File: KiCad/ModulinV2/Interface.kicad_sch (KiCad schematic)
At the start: 46 parts, among them IC3 ADS7041IDCUR, IC4 ADS7041IDCUR, IC5 ADS7866IDBVT, IC6 ADS7866IDBVT, IC7 DAC60501ZDGSR, IC8 DAC60501ZDGSR

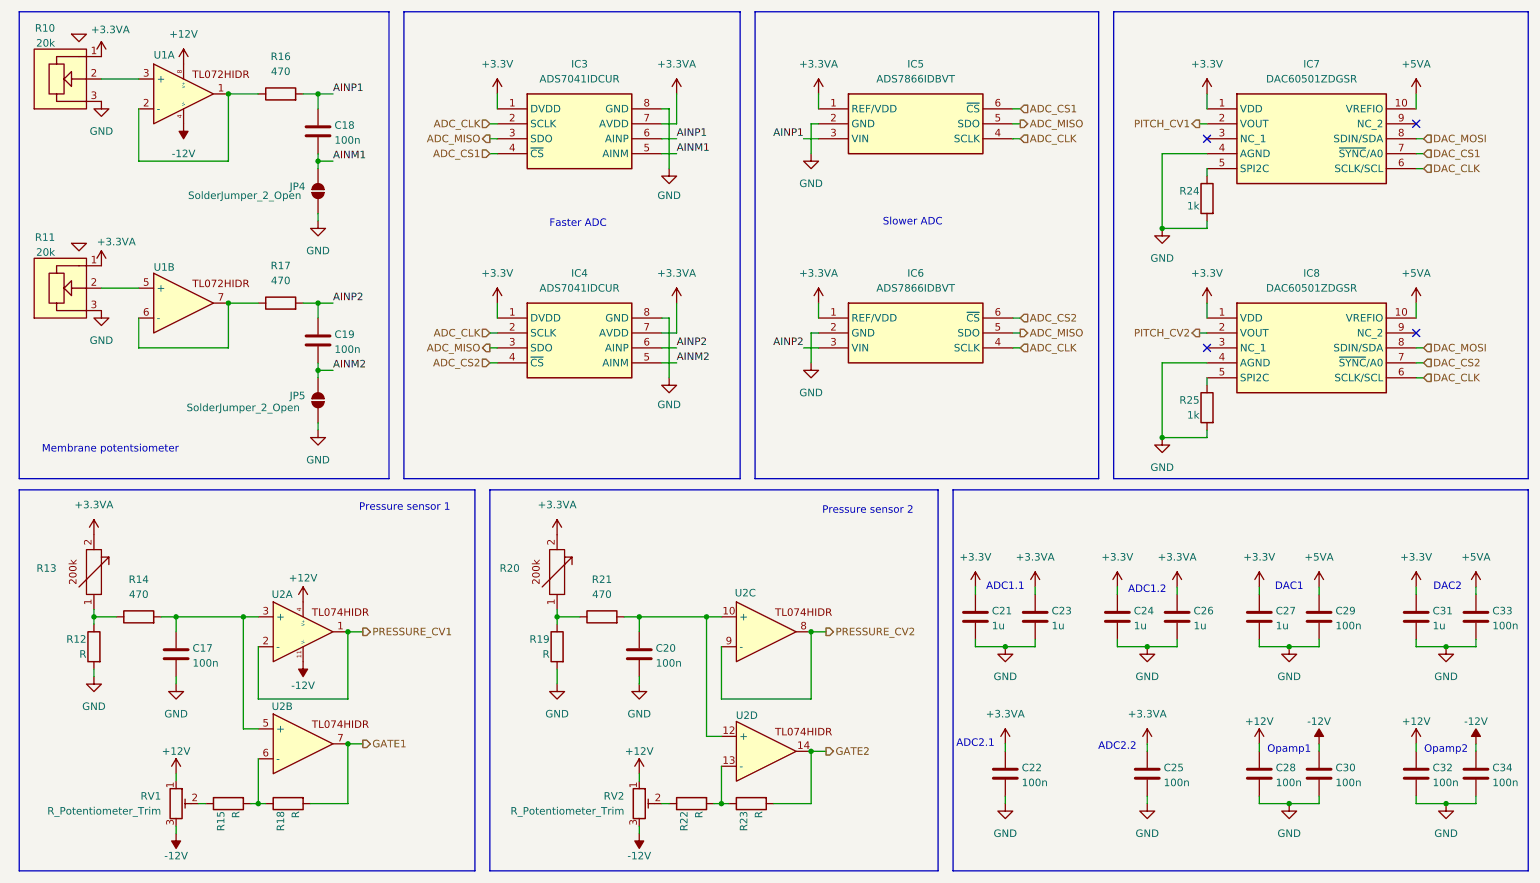
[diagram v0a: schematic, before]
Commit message: Added 4k7 pullups to I2C lines
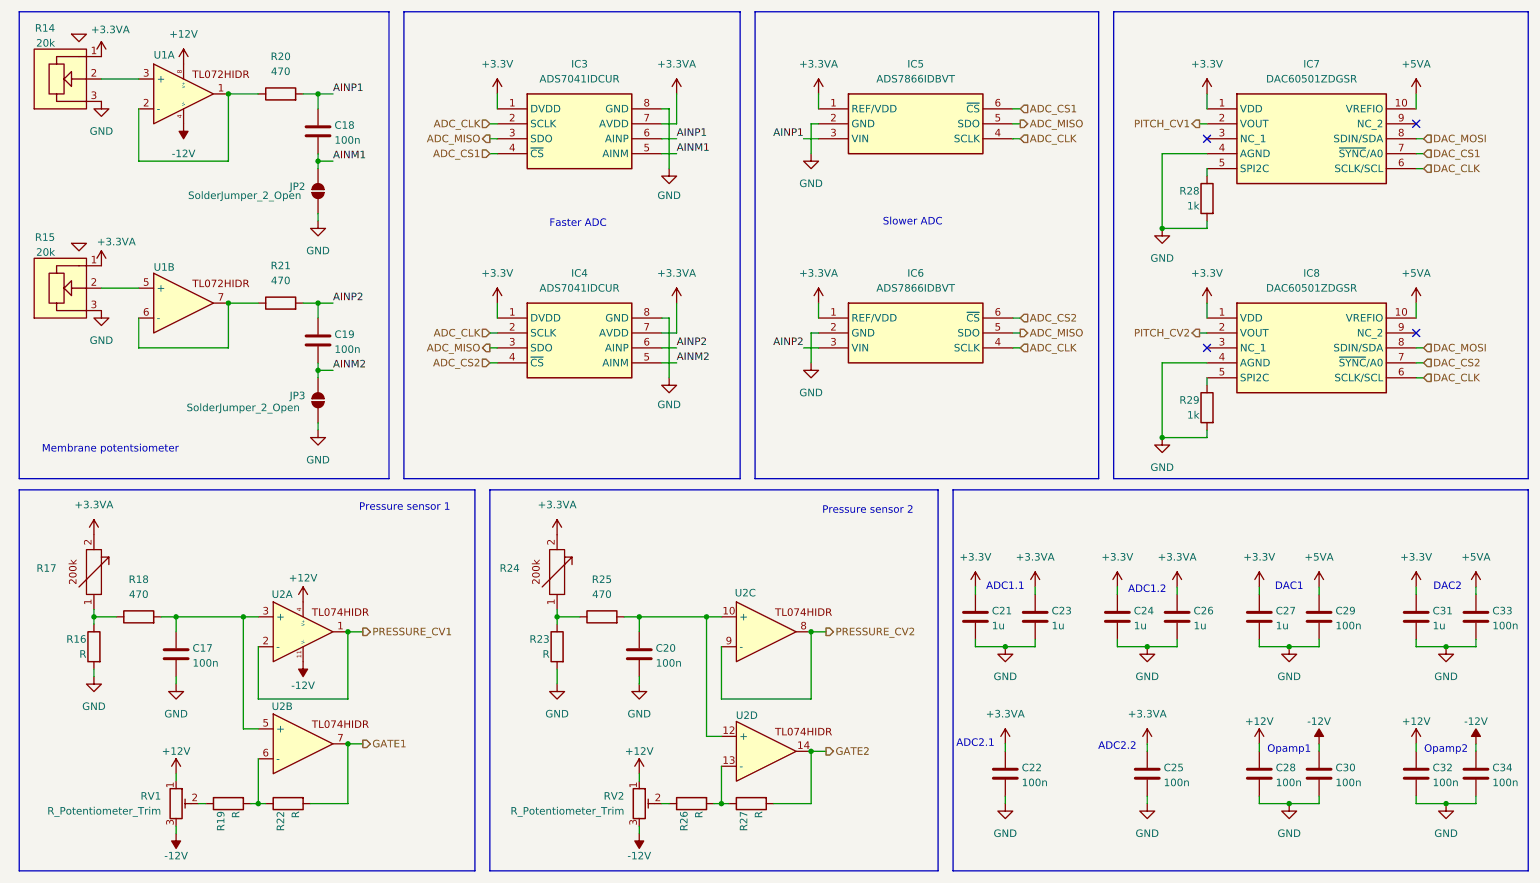
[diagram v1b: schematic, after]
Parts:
- renumbered JP4 to JP2, JP5 to JP3, R10 to R14, R11 to R15, R12 to R16, R13 to R17, R14 to R18, R15 to R19, R16 to R20, R17 to R21, R18 to R22, R19 to R23, R20 to R24, R21 to R25, R22 to R26, R23 to R27, R24 to R28, R25 to R29

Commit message: Added wave selection jumpers for testing
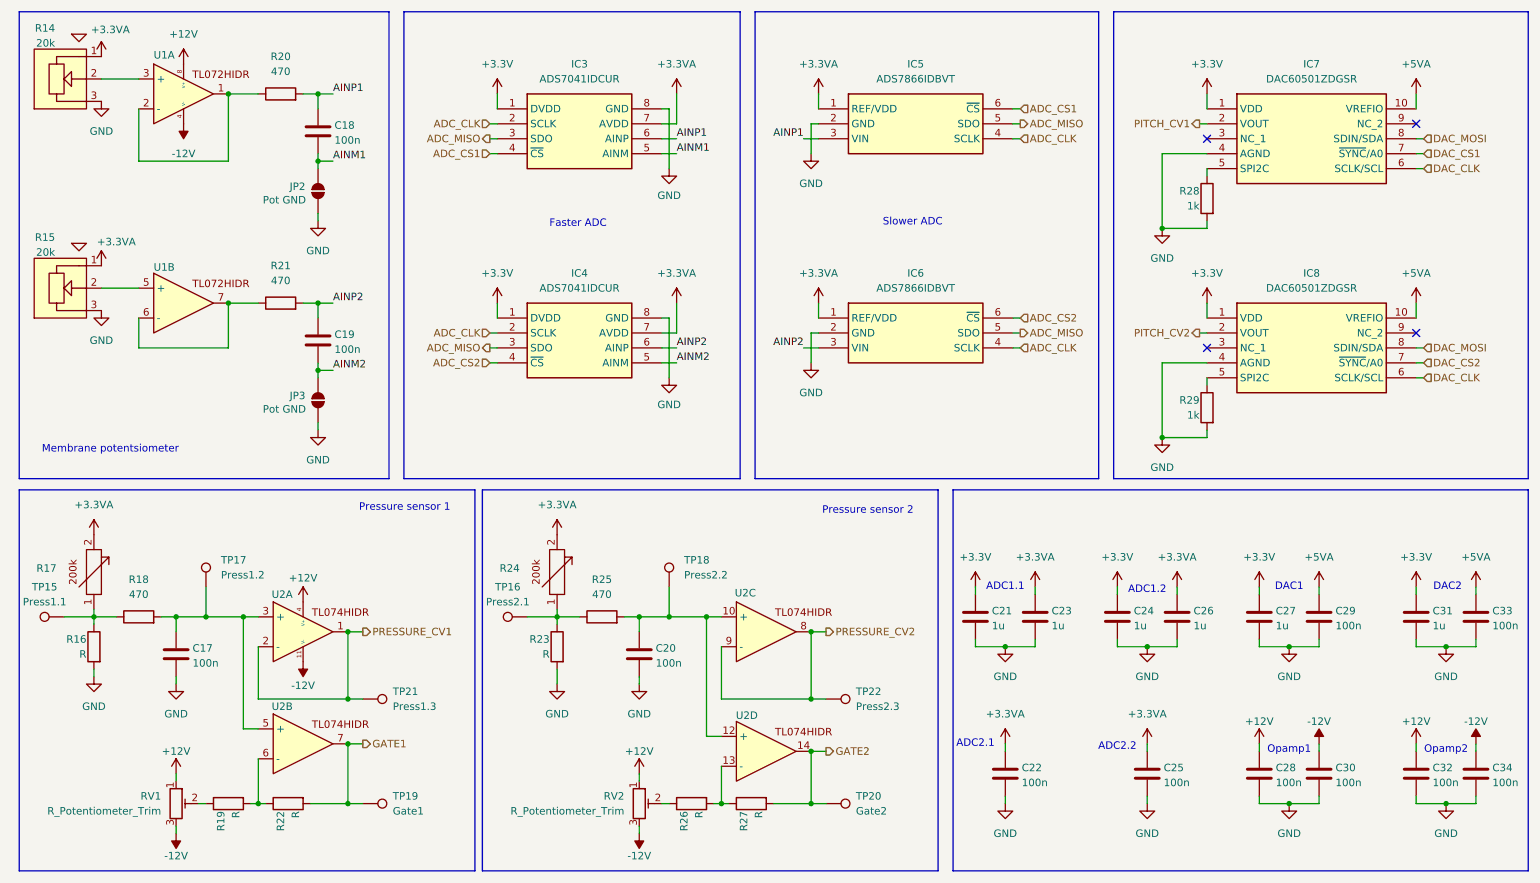
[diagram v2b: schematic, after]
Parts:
- added TP15: Press1.1, symbol Connector:TestPoint
- added TP16: Press2.1, symbol Connector:TestPoint
- added TP17: Press1.2, symbol Connector:TestPoint
- added TP18: Press2.2, symbol Connector:TestPoint
- added TP19: Gate1, symbol Connector:TestPoint
- added TP20: Gate2, symbol Connector:TestPoint
- added TP21: Press1.3, symbol Connector:TestPoint
- added TP22: Press2.3, symbol Connector:TestPoint
- JP2, JP3: value SolderJumper_2_Open -> Pot GND
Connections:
- net GATE1: now also TP19.1
- net GATE2: now also TP20.1
- net PRESSURE_CV1: now also TP21.1
- net PRESSURE_CV2: now also TP22.1
- net at R16.1, R17.1, R18.1: now also TP15.1
- net at R23.1, R24.1, R25.1: now also TP16.1
- net at C20.1, R25.2, U2.10 (+)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: now also TP18.1
- net at C17.1, R18.2, U2.3 (+)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: now also TP17.1

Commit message: Revert "Modified selection LED schematic and supply caps"
This reverts commit f7ca9d31056dcb2cadf4048ae59e1f5625a2aefa.
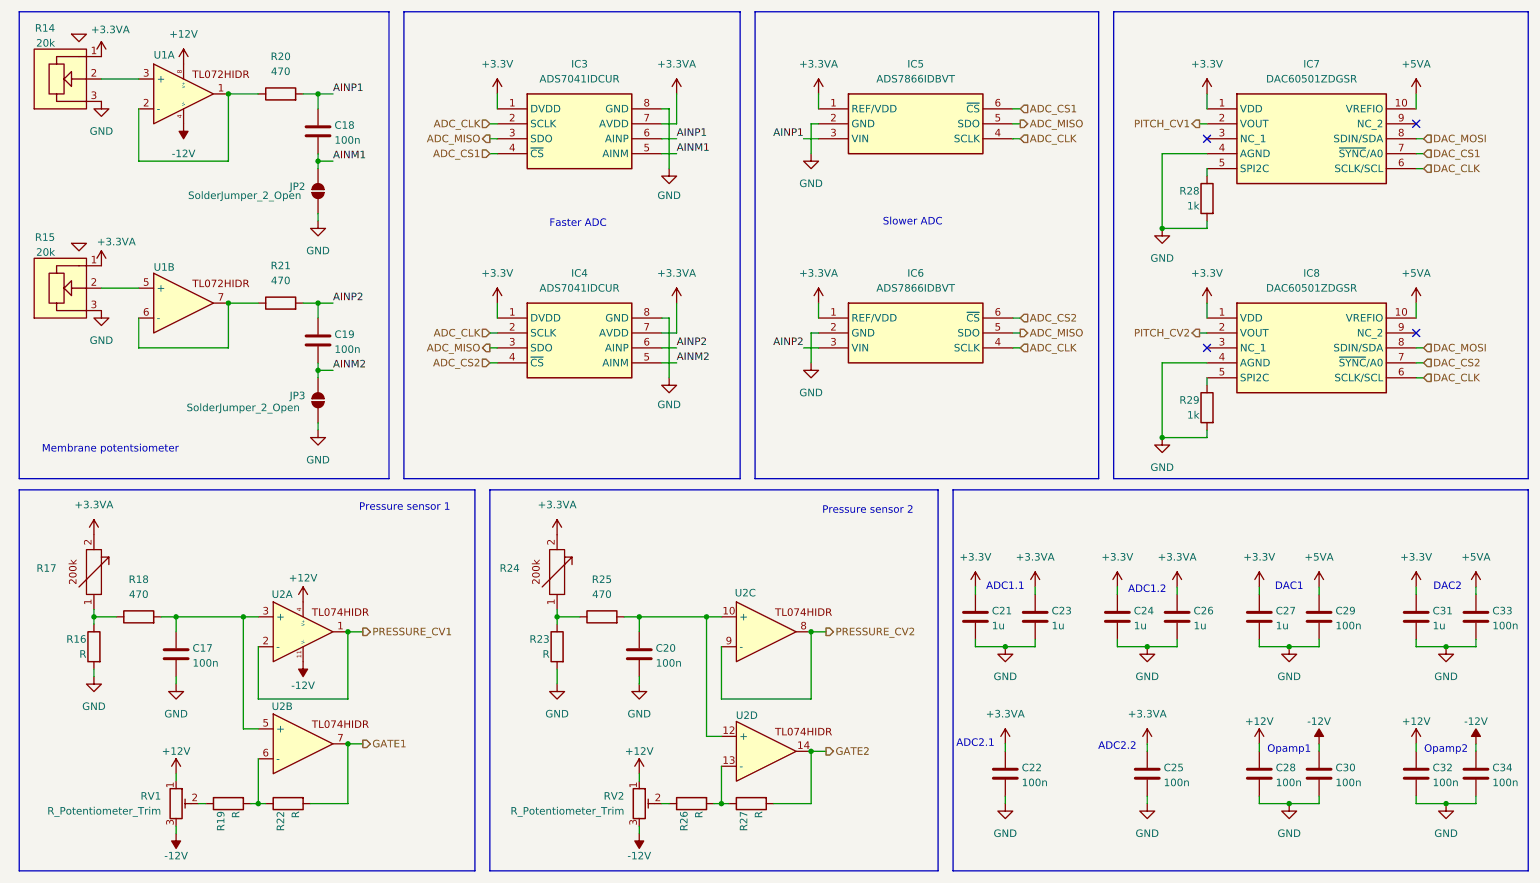
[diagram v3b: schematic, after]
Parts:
- removed TP15: Press1.1, symbol Connector:TestPoint
- removed TP16: Press2.1, symbol Connector:TestPoint
- removed TP17: Press1.2, symbol Connector:TestPoint
- removed TP18: Press2.2, symbol Connector:TestPoint
- removed TP19: Gate1, symbol Connector:TestPoint
- removed TP20: Gate2, symbol Connector:TestPoint
- removed TP21: Press1.3, symbol Connector:TestPoint
- removed TP22: Press2.3, symbol Connector:TestPoint
- JP2, JP3: value Pot GND -> SolderJumper_2_Open
